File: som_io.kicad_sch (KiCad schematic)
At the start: 1 part, among them J1 Hermaphroditic_Molex_203456-0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

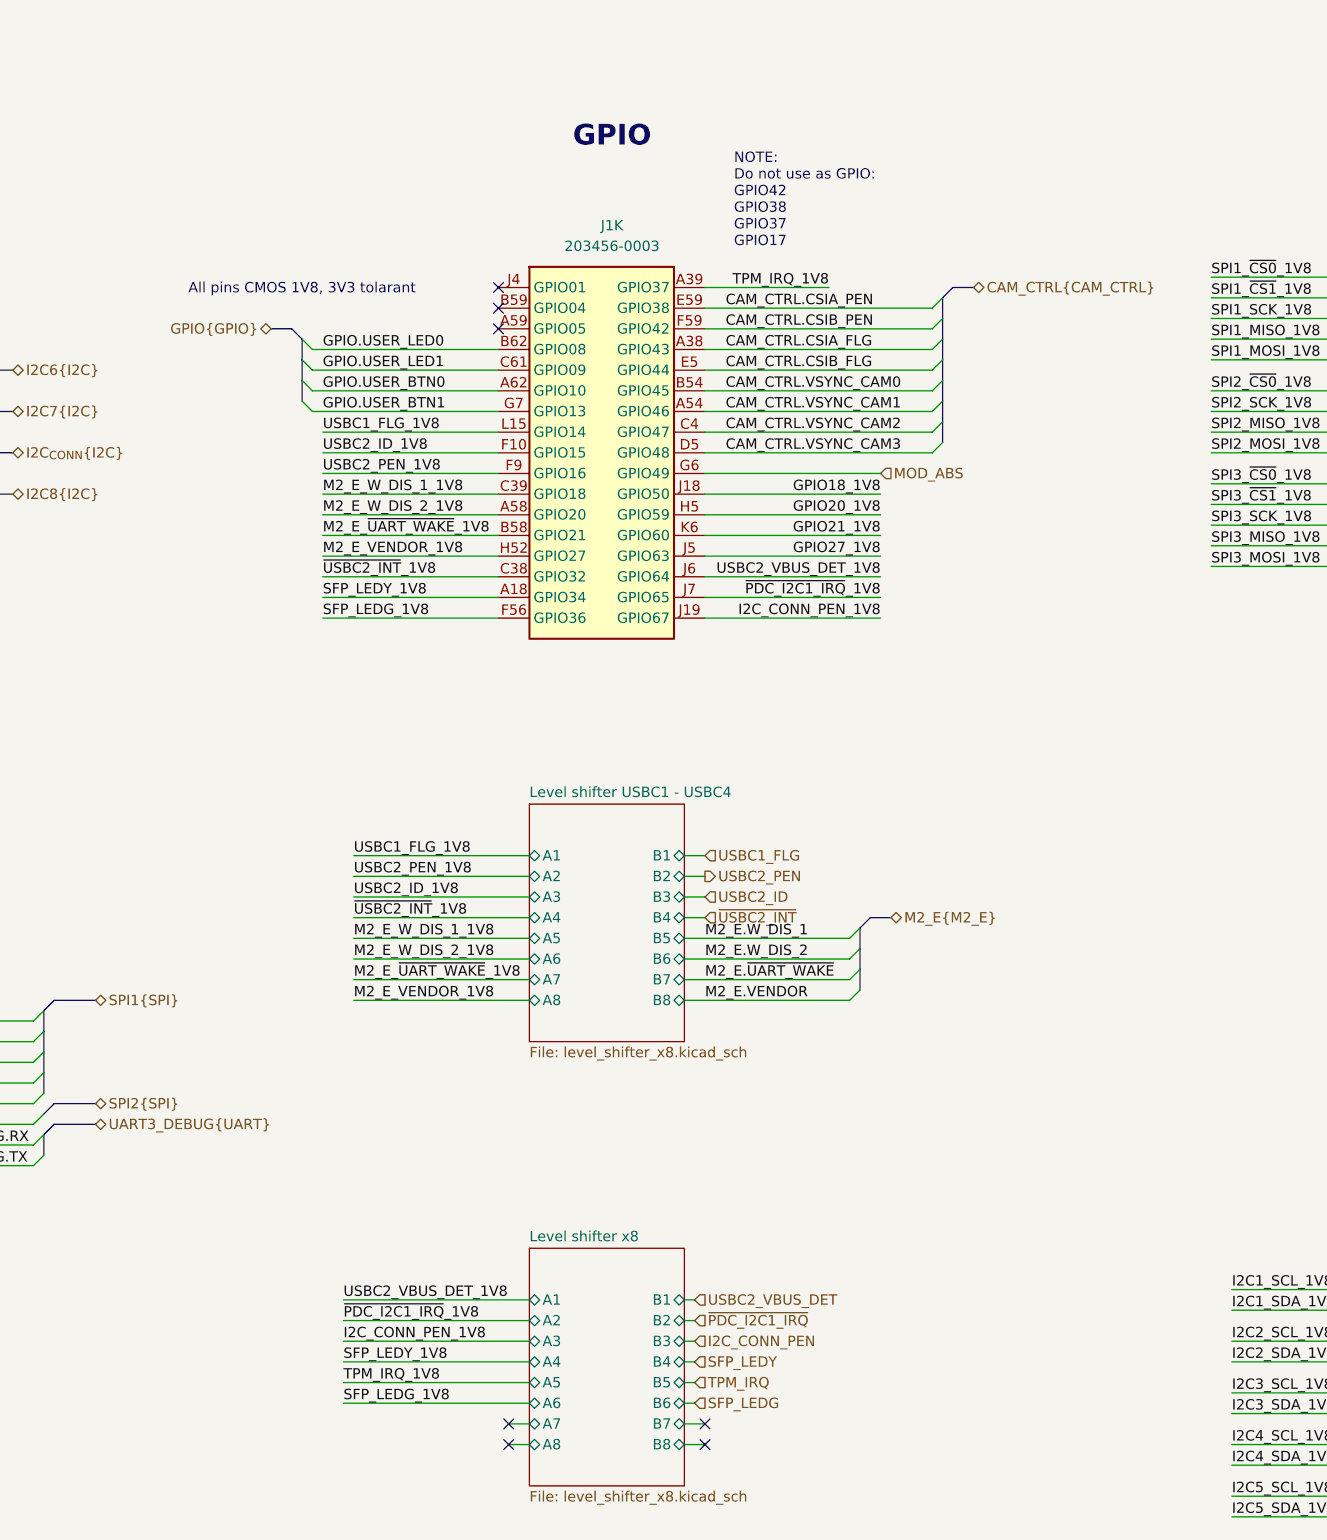
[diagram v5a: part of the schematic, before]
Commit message: [#85326] Fix Thor symbol, Free reserved GPIOs
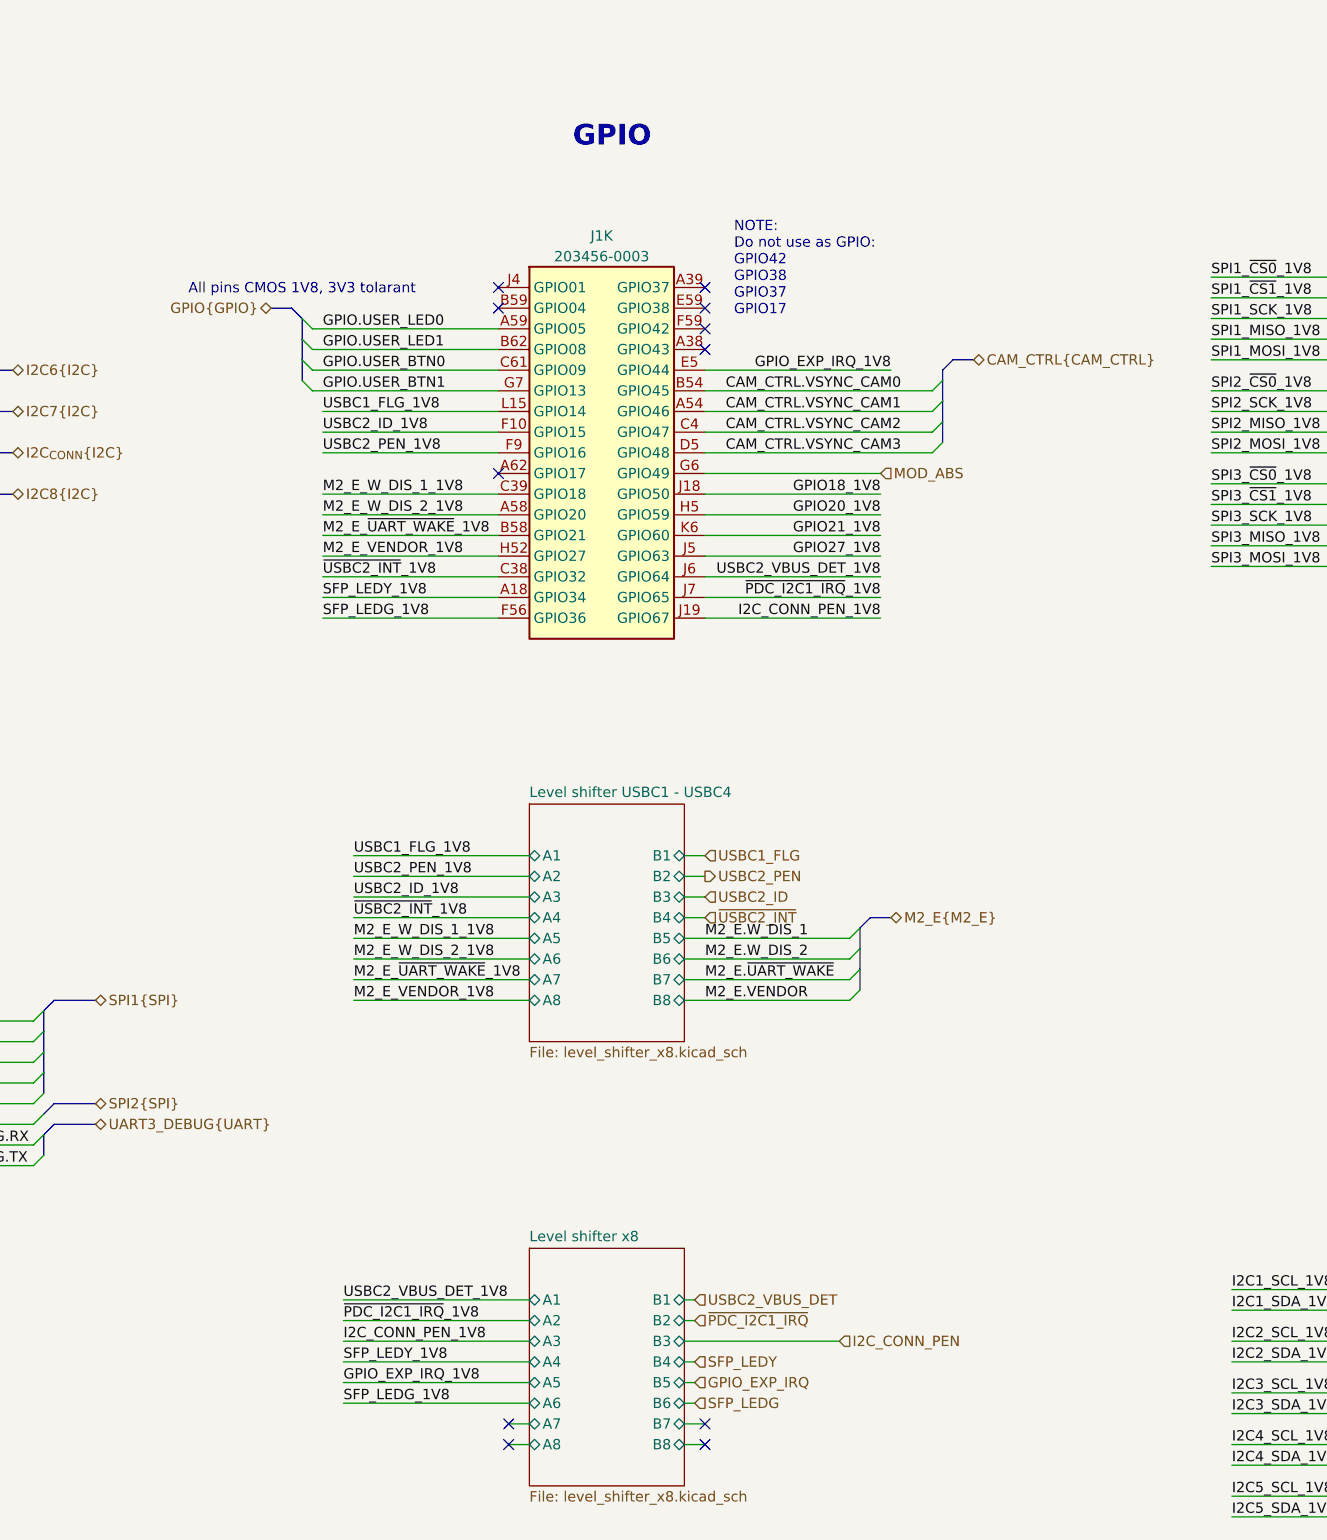
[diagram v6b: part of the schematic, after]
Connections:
- net GPIO.USER_BTN0: now also J1.C61 (GPIO09); no longer J1.A62 (GPIO10)
- net GPIO.USER_LED0: now also J1.A59 (GPIO05); no longer J1.B62 (GPIO08)
- net GPIO.USER_LED1: now also J1.B62 (GPIO08); no longer J1.C61 (GPIO09)
- net CAM_CTRL.CSIA_FLG: no longer names the net of J1.A38 (GPIO43)
- net CAM_CTRL.CSIA_PEN: no longer names the net of J1.E59 (GPIO38)
- net CAM_CTRL.CSIB_FLG renamed GPIO_EXP_IRQ_1V8
- net CAM_CTRL.CSIB_PEN: no longer names the net of J1.F59 (GPIO42)
- net TPM_IRQ_1V8: no longer names the net of J1.A39 (GPIO37)
- no-connect marks 62 -> 66

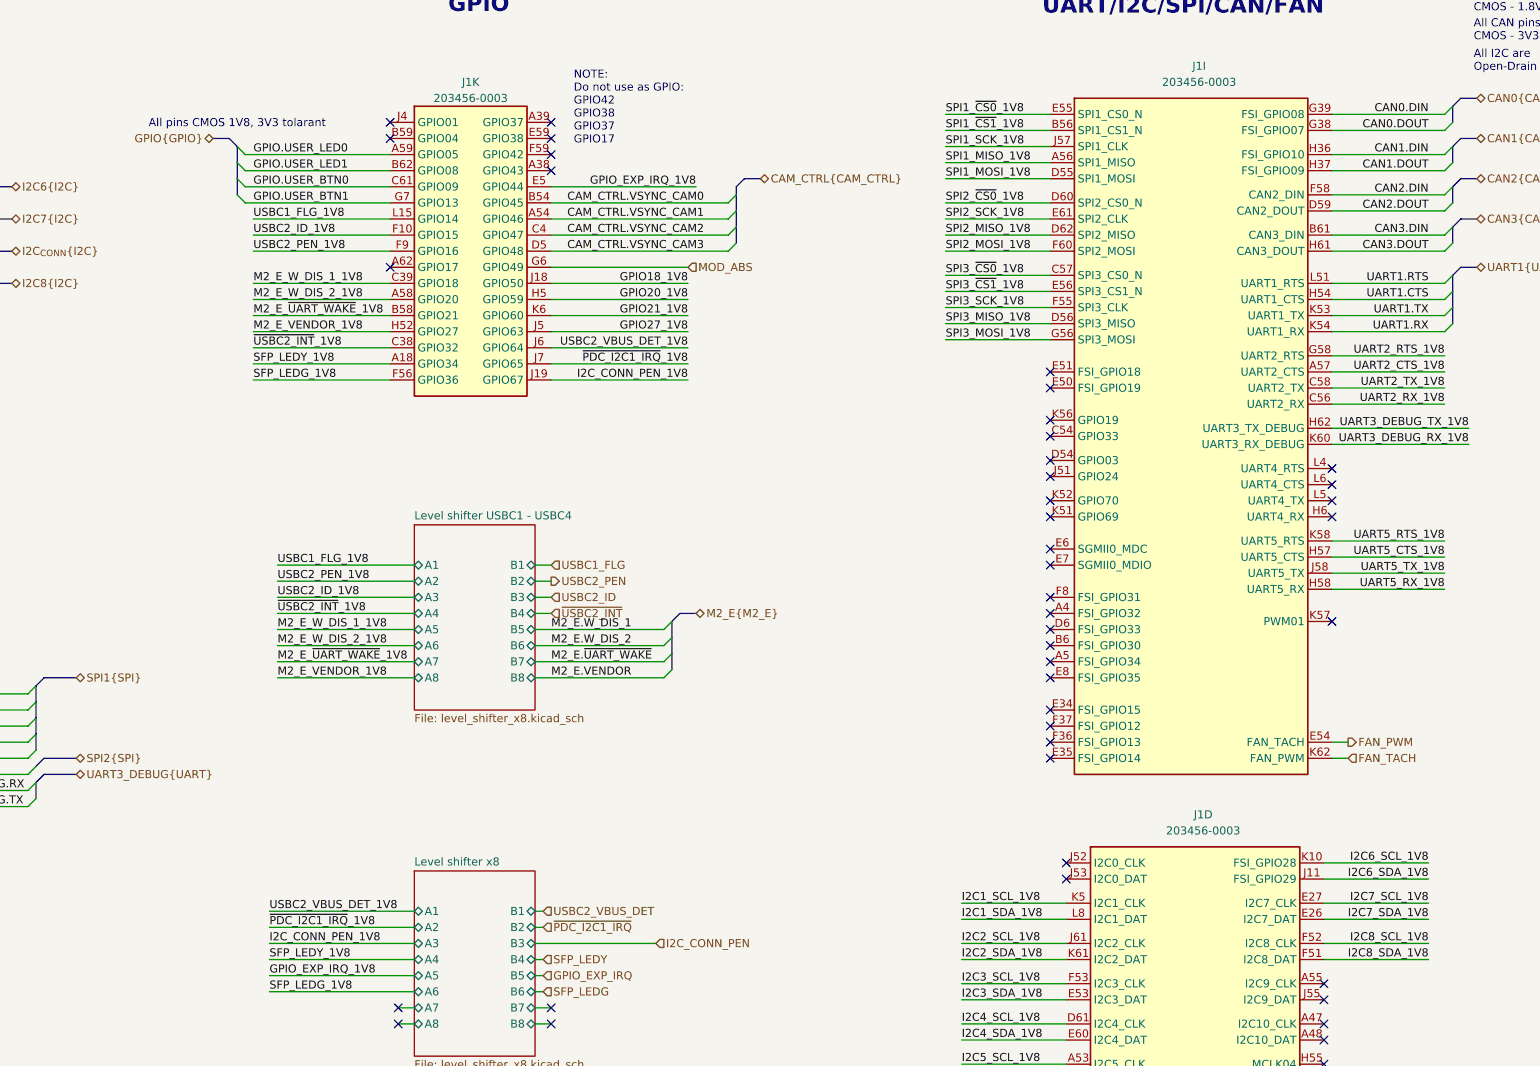
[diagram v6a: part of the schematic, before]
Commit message: [#85326] Fix incorrect GPIO voltage levels, add SFP related TVS
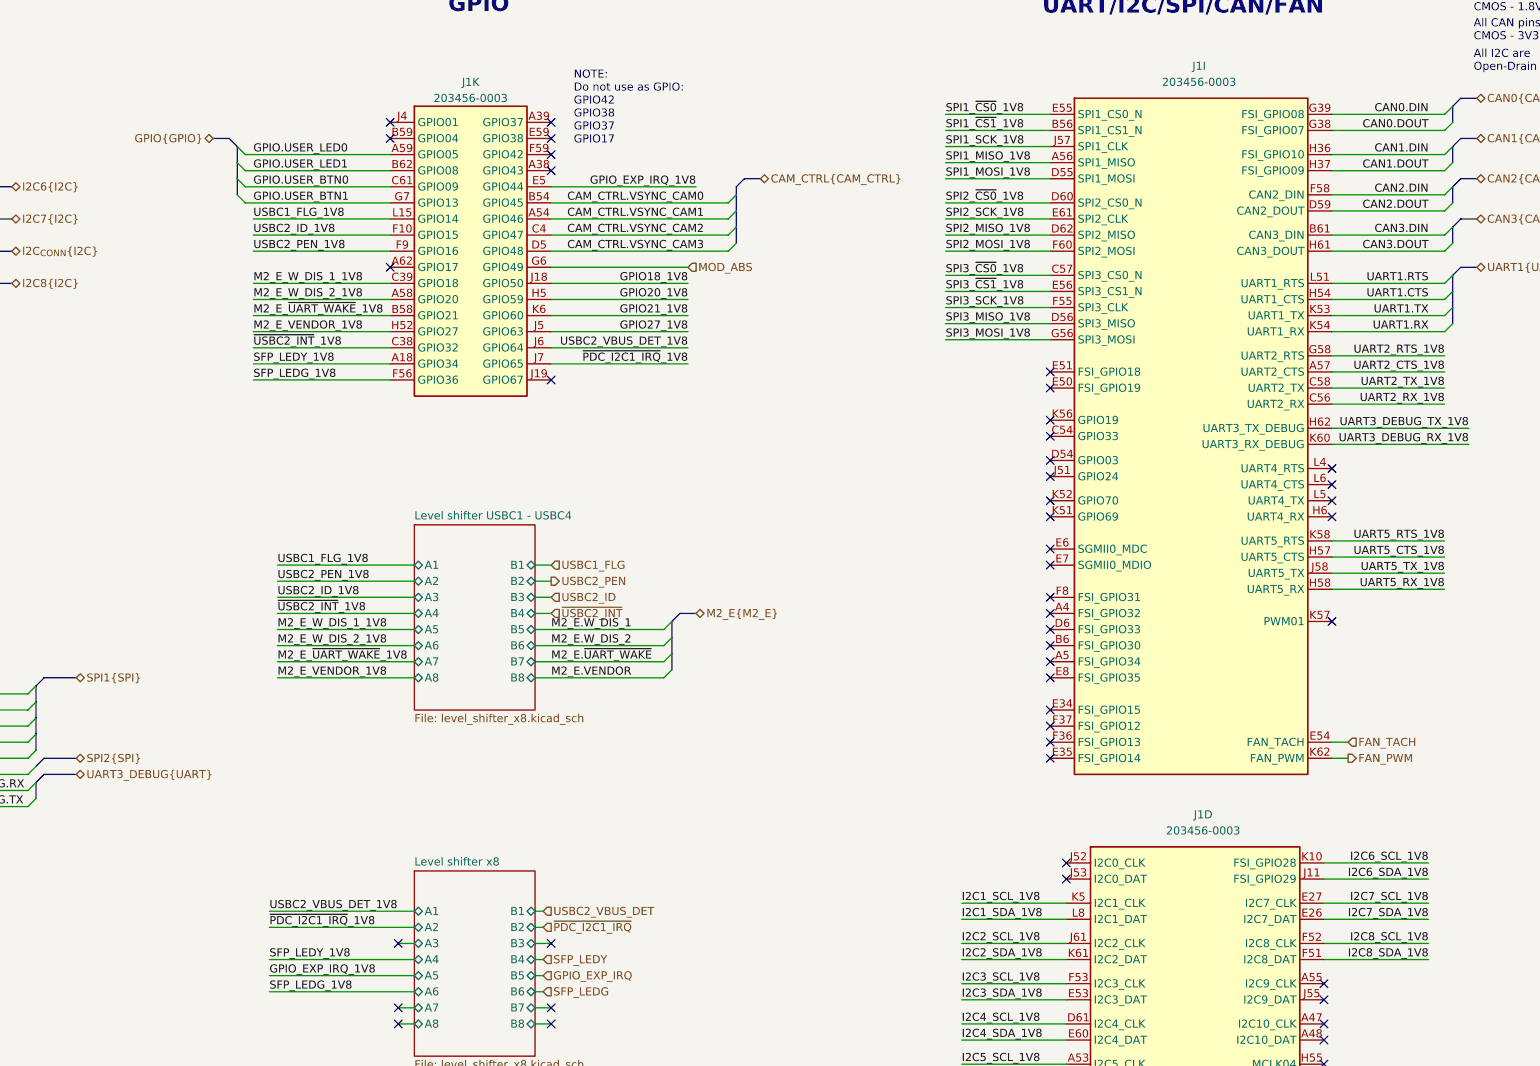
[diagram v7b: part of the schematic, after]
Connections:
- net FAN_PWM: now also J1.K62 (FAN_PWM); no longer J1.E54 (FAN_TACH)
- net FAN_TACH: now also J1.E54 (FAN_TACH); no longer J1.K62 (FAN_PWM)
- net I2C_CONN_PEN_1V8: no longer names the net of J1.J19 (GPIO67)
- no-connect marks 66 -> 69
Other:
- note removed: "All pins CMOS 1V8, 3V3 tolarant"
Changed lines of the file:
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@@
 		)
 	)
-	(text "All pins CMOS 1V8, 3V3 tolarant"
-		(exclude_from_sim no)
-		(at 190.5 35.814 0)
-		(effects
-			(font
-				(size 1.27 1.27)
-			)
-		)
-	)
 	(text "GPIO"
 		(exclude_from_sim no)
@@
 	)
 	(no_connect
+		(at 240.03 76.2)
+	)
+	(no_connect
 		(at 240.03 229.87)
 	)
@@
 	)
 	(no_connect
+		(at 215.9 165.1)
+	)
+	(no_connect
 		(at 318.77 123.19)
 	)
@@
 	)
 	(no_connect
+		(at 240.03 165.1)
+	)
+	(no_connect
 		(at 361.95 173.99)
 	)
@@
 	(wire
 		(pts
-			(xy 365.76 133.35) (xy 363.22 133.35)
+			(xy 365.76 135.89) (xy 363.22 135.89)
 		)
 		(stroke
@@
 		)
 	)
+	(wire
+		(pts
+			(xy 215.9 165.1) (xy 218.44 165.1)
+		)
+		(stroke
+			(width 0)
+			(type default)
+		)
+	)
 	(bus
 		(pts
@@
 	(wire
 		(pts
-			(xy 365.76 135.89) (xy 363.22 135.89)
+			(xy 365.76 133.35) (xy 363.22 133.35)
 		)
 		(stroke
@@
 	(wire
 		(pts
-			(xy 240.03 76.2) (xy 261.62 76.2)
-		)
-		(stroke
-			(width 0)
-			(type default)
-		)
-	)
-	(wire
-		(pts
 			(xy 237.49 217.17) (xy 248.92 217.17)
 		)
@@
 	(wire
 		(pts
-			(xy 256.54 165.1) (xy 237.49 165.1)
-		)
-		(stroke
-			(width 0)
-			(type default)
-		)
-	)
-	(wire
-		(pts
 			(xy 302.26 48.26) (xy 318.77 48.26)
 		)
@@
 		)
 	)
-	(wire
+	(bus
 		(pts
-			(xy 195.58 165.1) (xy 218.44 165.1)
+			(xy 77.47 133.35) (xy 74.93 133.35)
 		)
 		(stroke
@@
 		)
 	)
-	(bus
+	(wire
 		(pts
-			(xy 77.47 133.35) (xy 74.93 133.35)
+			(xy 237.49 165.1) (xy 240.03 165.1)
 		)
 		(stroke
@@
 		)
 	)
-	(label "I2C_CONN_PEN_1V8"
-		(at 261.62 76.2 180)
-		(effects
-			(font
-				(size 1.27 1.27)
-			)
-			(justify right bottom)
-		)
-	)
 	(label "UART2.TX"
 		(at 60.96 130.81 0)
@@
 		)
 	)
-	(label "I2C_CONN_PEN_1V8"
-		(at 195.58 165.1 0)
-		(effects
-			(font
-				(size 1.27 1.27)
-			)
-			(justify left bottom)
-		)
-	)
 	(label "SPI3_MOSI_1V8"
 		(at 20.32 217.17 0)
@@
 		)
 	)
-	(hierarchical_label "I2C_CONN_PEN"
-		(shape input)
-		(at 256.54 165.1 0)
-		(effects
-			(font
-				(size 1.27 1.27)
-			)
-			(justify left)
-		)
-	)
 	(hierarchical_label "GPIO{GPIO}"
 		(shape bidirectional)
@@
 	(hierarchical_label "FAN_PWM"
 		(shape output)
-		(at 365.76 133.35 0)
+		(at 365.76 135.89 0)
 		(effects
 			(font
@@
 	(hierarchical_label "FAN_TACH"
 		(shape input)
-		(at 365.76 135.89 0)
+		(at 365.76 133.35 0)
 		(effects
 			(font

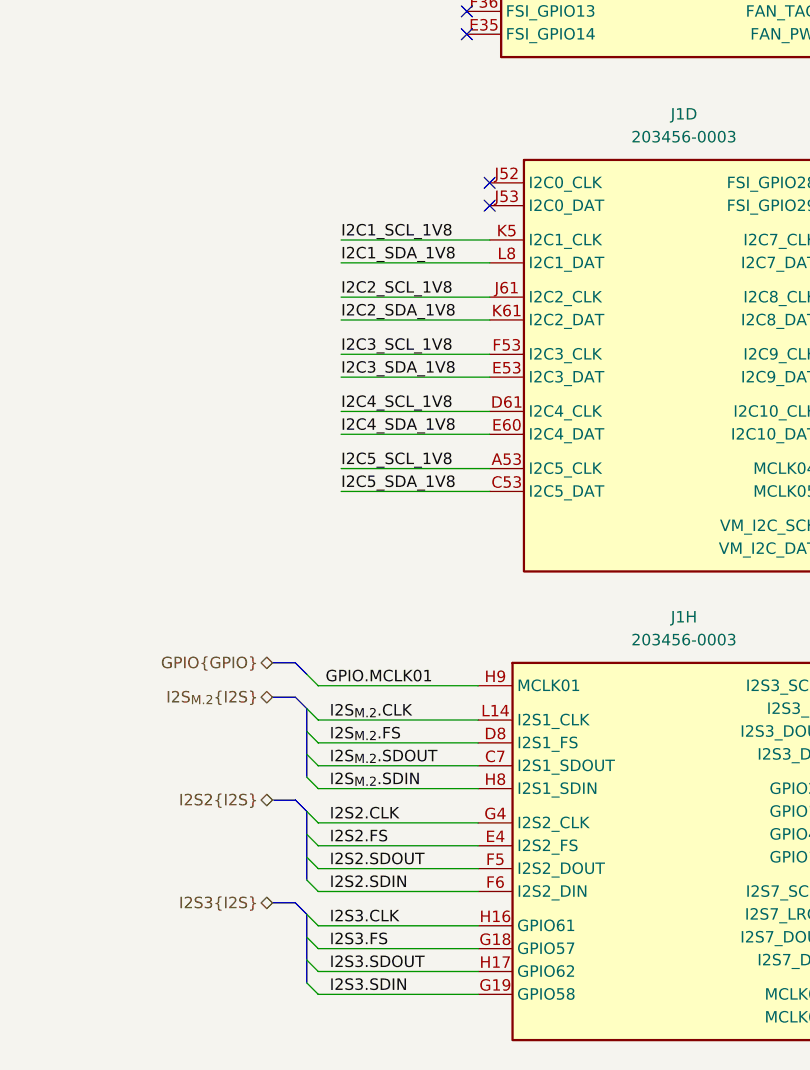
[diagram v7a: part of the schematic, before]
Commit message: [#85326] Fix FAN signals, add testpoints, add DP capaciors, fix optional JTAG connector
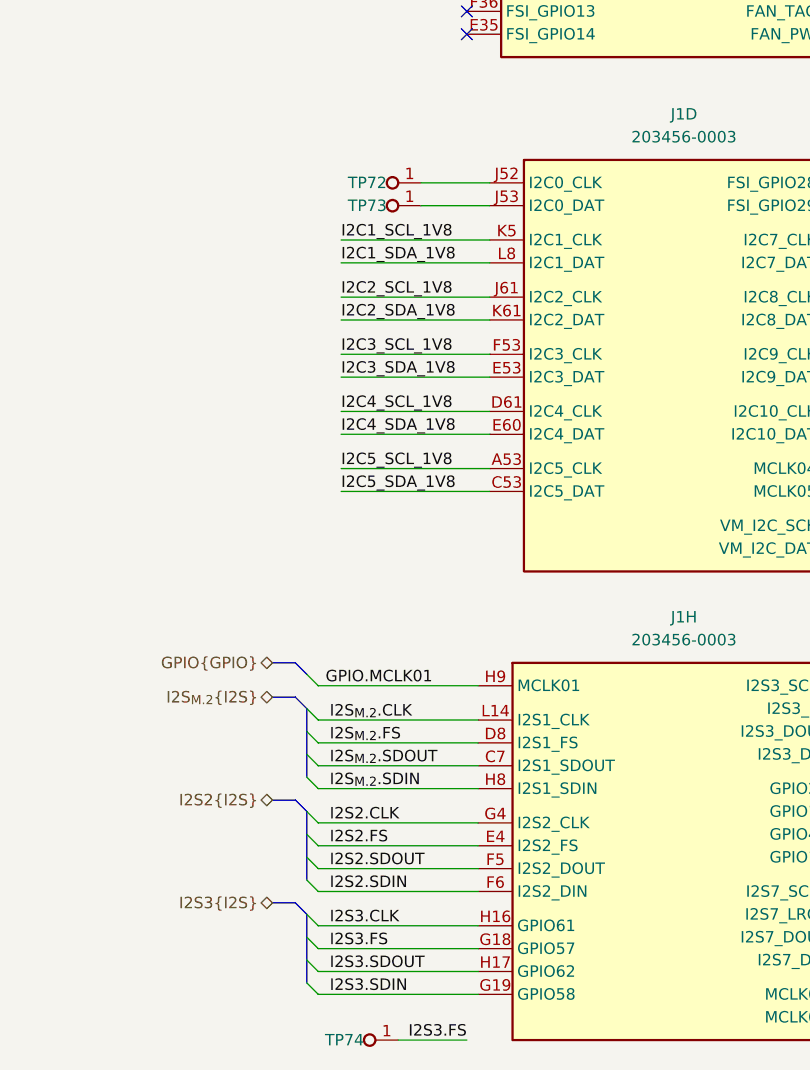
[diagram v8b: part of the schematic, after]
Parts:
- added TP72, TP73, TP74: TP_0.75mm_SMD, antmicro-footprints:TP_SMD_0.75mm, symbol antmicroTestPoints:TP_0.75mm_SMD
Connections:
- net I2S3.FS: now also TP74.1
- net at J1.J52 (I2C0_CLK): now also TP72.1
- net at J1.J53 (I2C0_DAT): now also TP73.1
- no-connect marks 69 -> 67
